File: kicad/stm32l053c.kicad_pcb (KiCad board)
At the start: 2 copper layers, 53 x 35 mm, 32 parts, among them P1 SWD, P2 PWR, Q1 Q_NMOS_GSD, SW1 SW_PUSH, SW2 SW_PUSH, SW3 SW_PUSH, U1 STM32L053C8_LQFP48, U2 TLV61225, Y1 Crystal

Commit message: Enclosure sizes
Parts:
- added REF**: MountingHole_2.2mm_M2, Mounting_Holes:MountingHole_2.2mm_M2, F.Cu at (152.0, 118.1)
- added REF**: MountingHole_2.2mm_M2, Mounting_Holes:MountingHole_2.2mm_M2, F.Cu at (131.0, 118.1)
- added REF**: MountingHole_2.2mm_M2, Mounting_Holes:MountingHole_2.2mm_M2, F.Cu at (154.0, 104.6)
- added REF**: MountingHole_2.2mm_M2, Mounting_Holes:MountingHole_2.2mm_M2, F.Cu at (132.0, 104.6)
- DS1: footprint theapi:ZEBRA-12 -> ZEBRA-12
- moved SW3 2.09 mm to (164.0, 111.6)
- moved SW1 0.78 mm to (121.5, 111.6)
- moved SW2 0.78 mm to (141.5, 111.6)

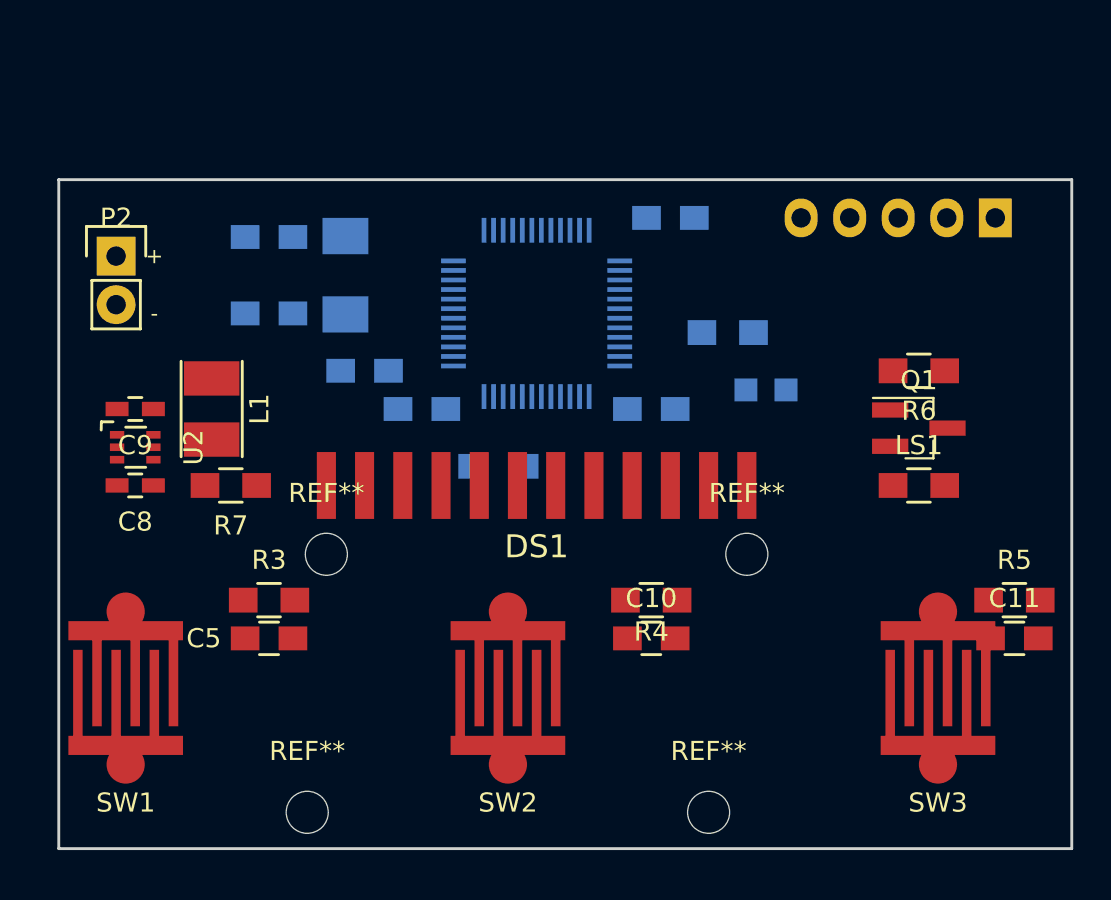
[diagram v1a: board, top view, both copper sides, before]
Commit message: Layout to fit the enclosure
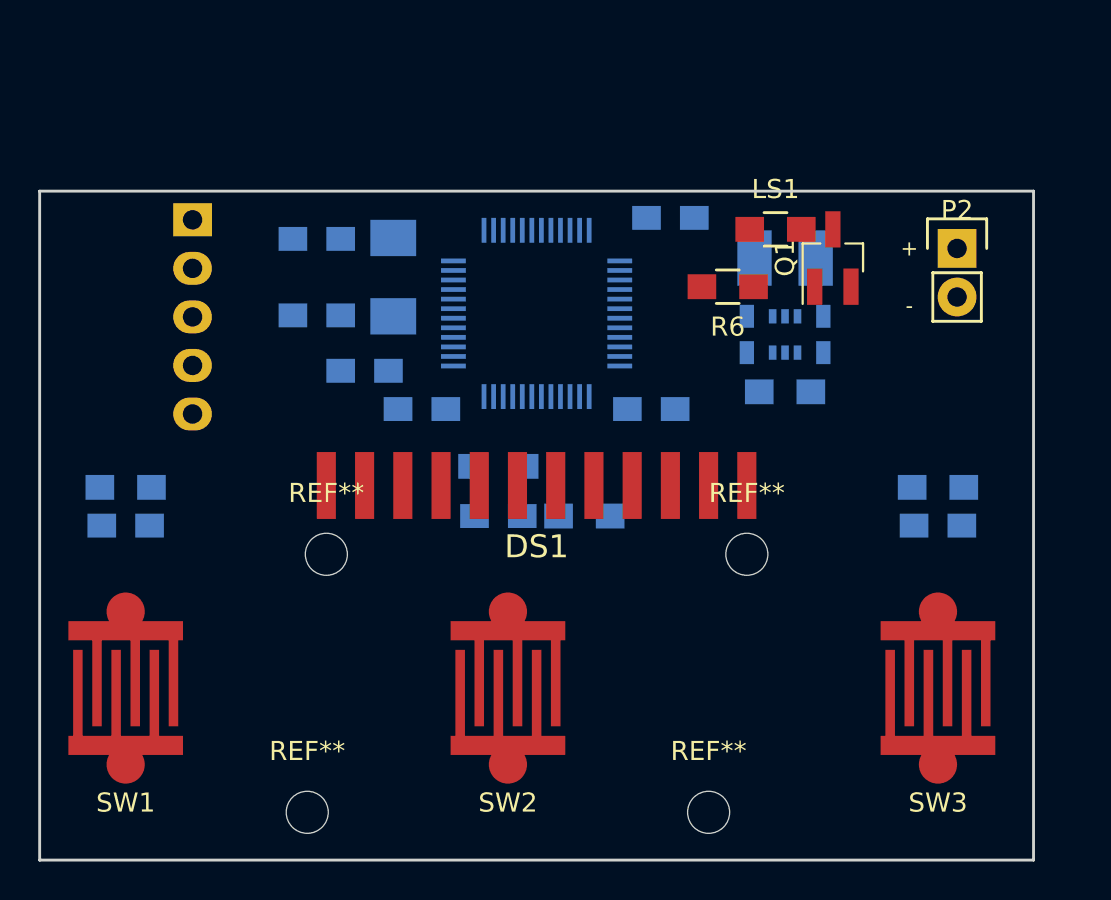
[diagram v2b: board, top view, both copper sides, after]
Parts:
- removed D1: LED, LEDs:LED_0805
- removed R1: 820, Resistors_SMD:R_0805_HandSoldering
- C10, C11, C5, C8, C9, L1, R3, R4, R5, R7, U2: moved to B.Cu
- moved P2 44.0 mm to (165.0, 88.6)
- moved P1 42.0 mm to (125.0, 87.1), turned to 180 degrees
- moved C9 36.2 mm to (158.0, 93.1), turned to 270 degrees
- moved U2 34.5 mm to (156.0, 93.1), turned to 180 degrees
- moved C8 33.0 mm to (154.0, 93.1), turned to 270 degrees
- moved L1 31.0 mm to (156.0, 89.1), turned to 180 degrees
- moved R7 29.4 mm to (156.0, 96.1)
- moved REF** 15.4 mm to (143.0, 108.6)
- moved LS1 15.4 mm to (155.5, 87.6)
- moved R6 10.9 mm to (153.0, 90.6)
- moved C10 10.2 mm to (141.0, 102.6), turned to 180 degrees
- moved Q1 9.97 mm to (158.5, 89.1), turned to 90 degrees
- moved C5 9.54 mm to (121.5, 103.1), turned to 180 degrees
- moved R3 9.54 mm to (121.5, 101.1), turned to 180 degrees
- moved C11 7.13 mm to (164.0, 103.1)
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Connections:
- U1 pad 10: (no net) -> Net-(U1-Pad10)
- U1 pad 14: (no net) -> Net-(U1-Pad14)
- U1 pad 2: (no net) -> Net-(U1-Pad2)
- U1 pad 20: (no net) -> Net-(U1-Pad20)
- U1 pad 21: (no net) -> Net-(U1-Pad21)
- U1 pad 22: (no net) -> Net-(U1-Pad22)
- U1 pad 25: (no net) -> Net-(U1-Pad25)
- U1 pad 26: (no net) -> Net-(U1-Pad26)
- U1 pad 27: (no net) -> Net-(U1-Pad27)
- U1 pad 32: (no net) -> Net-(U1-Pad32)
- U1 pad 33: (no net) -> Net-(U1-Pad33)
- U1 pad 38: (no net) -> Net-(U1-Pad38)
- U1 pad 43: (no net) -> Net-(U1-Pad43)
- U1 pad 45: (no net) -> Net-(U1-Pad45)
- U1 pad 5: (no net) -> Net-(U1-Pad5)
- U1 pad 6: (no net) -> Net-(U1-Pad6)
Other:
- board size 53 x 35 mm -> 52 x 35 mm

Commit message: Layout (WIP)
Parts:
- added D1: D_Schottky, Diodes_SMD:D_0805, B.Cu at (126.0, 100.6)
- added D2: D_Schottky, Diodes_SMD:D_0805, B.Cu at (154.0, 96.6)
- added D3: D_Schottky, Diodes_SMD:D_0805, B.Cu at (159.0, 101.6)
- added D4: D, Diodes_SMD:D_0805, F.Cu at (162.0, 89.6)
- added R1: 0, Resistors_SMD:R_0805_HandSoldering, F.Cu at (151.0, 92.6)
- added U3: um66t, TO_SOT_Packages_THT:TO-92_Inline_Narrow_Oval, F.Cu at (164.0, 96.6)
- DS1: footprint ZEBRA-12 -> theapi:ZEBRA-12
- Q1: value Q_NMOS_GSD -> Q_PNP_BEC
- R2: moved to F.Cu
- SW3: footprint SW_PCB -> theapi:SW_PCB
- moved L1 29.8 mm to (126.5, 93.1), turned to 270 degrees
- moved C9 27.6 mm to (130.5, 91.1), turned to 0 degrees
- moved U2 25.5 mm to (130.5, 93.1), turned to 270 degrees
- moved C8 23.6 mm to (130.5, 95.1), turned to 0 degrees
- moved R7 22.7 mm to (133.5, 93.1), turned to 90 degrees
- moved C10 19.3 mm to (159.2, 96.1)
- moved C4 17.2 mm to (150.0, 88.6), turned to 180 degrees
- moved R4 14.5 mm to (159.3, 98.3)
- moved R2 11.6 mm to (143.0, 88.6)
- moved Y1 9.62 mm to (137.0, 80.6)
- moved C6 9.06 mm to (132.5, 83.1)
- moved C7 9.06 mm to (132.5, 79.1)
- moved U1 0.60 mm to (143.0, 92.6), turned to 180 degrees
- moved P1 0.50 mm to (125.0, 87.6), turned to 270 degrees
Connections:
- LS1 pad 1: VDD -> +BATT
- R6 pad 2: /PB15 -> Net-(R1-Pad1)
- U1 pad 10: Net-(U1-Pad10) -> /WAKEUP_PIN1
- U1 pad 14: Net-(U1-Pad14) -> (no net)
- U1 pad 15: PA5 -> (no net)
- U1 pad 2: Net-(U1-Pad2) -> (no net)
- U1 pad 20: Net-(U1-Pad20) -> (no net)
- U1 pad 21: Net-(U1-Pad21) -> (no net)
- U1 pad 22: Net-(U1-Pad22) -> /BUZZER
- U1 pad 25: Net-(U1-Pad25) -> (no net)
- U1 pad 26: Net-(U1-Pad26) -> (no net)
- U1 pad 27: Net-(U1-Pad27) -> (no net)
- U1 pad 28: /PB15 -> /MELODY
- U1 pad 32: Net-(U1-Pad32) -> (no net)
- U1 pad 33: Net-(U1-Pad33) -> (no net)
- U1 pad 38: Net-(U1-Pad38) -> (no net)
- U1 pad 43: Net-(U1-Pad43) -> (no net)
- U1 pad 45: Net-(U1-Pad45) -> (no net)
- U1 pad 5: Net-(U1-Pad5) -> (no net)
- U1 pad 6: Net-(U1-Pad6) -> (no net)
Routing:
- net /LCD_COM2: track 0.00 -> 19.1 mm, vias 0 -> 1
- net /LCD_SEG0: track 0.00 -> 17.8 mm, vias 0 -> 1
- net /LCD_SEG6: track 0.00 -> 17.7 mm, vias 0 -> 1
- net /LCD_SEG2: track 0.00 -> 16.6 mm, vias 0 -> 1
- net /LCD_COM3: track 0.00 -> 16.6 mm, vias 0 -> 1
- net /LCD_SEG7: track 0.00 -> 16.4 mm, vias 0 -> 1
- net /LCD_SEG1: track 0.00 -> 15.6 mm, vias 0 -> 1
- net /LCD_SEG3: track 0.00 -> 11.8 mm, vias 0 -> 1
- net /LCD_SEG5: track 0.00 -> 11.8 mm, vias 0 -> 1
- net /LCD_COM0: track 0.00 -> 11.6 mm, vias 0 -> 1
- net /LCD_COM1: track 0.00 -> 11.2 mm, vias 0 -> 1
- net /LCD_SEG4: track 0.00 -> 8.05 mm, vias 0 -> 1

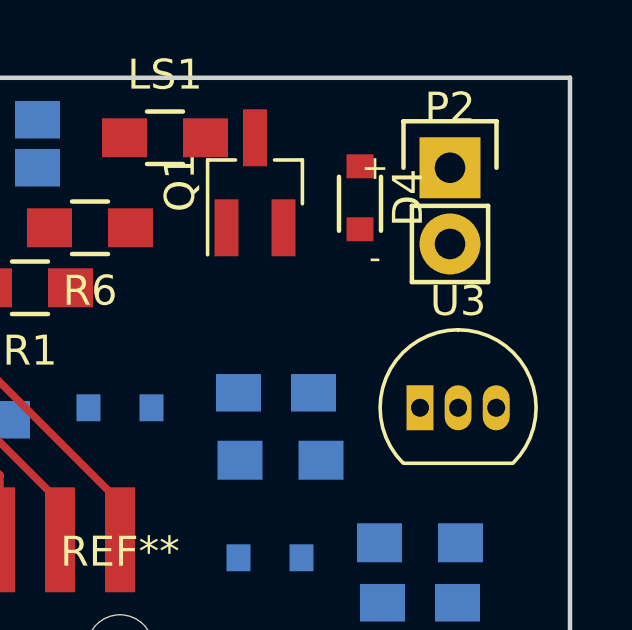
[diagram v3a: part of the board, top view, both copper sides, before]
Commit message: Fixed the melody output
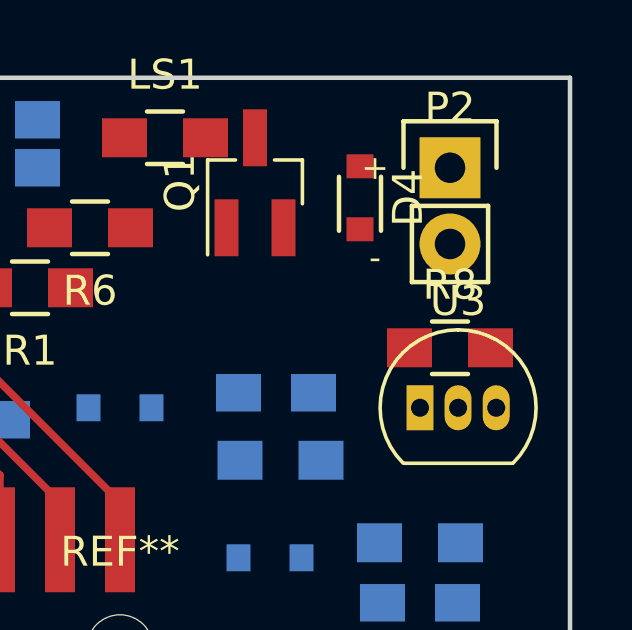
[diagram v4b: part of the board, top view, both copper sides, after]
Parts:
- added R8: 1K, Resistors_SMD:R_0805_HandSoldering, F.Cu at (165.0, 94.6)
- R6: value 1K -> 220
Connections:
- U1 pad 14: (no net) -> Net-(U1-Pad14)
- U1 pad 15: (no net) -> PA5
- U1 pad 2: (no net) -> Net-(U1-Pad2)
- U1 pad 20: (no net) -> Net-(U1-Pad20)
- U1 pad 21: (no net) -> Net-(U1-Pad21)
- U1 pad 25: (no net) -> /MELODY
- U1 pad 26: (no net) -> Net-(U1-Pad26)
- U1 pad 27: (no net) -> Net-(U1-Pad27)
- U1 pad 28: /MELODY -> Net-(U1-Pad28)
- U1 pad 32: (no net) -> Net-(U1-Pad32)
- U1 pad 33: (no net) -> Net-(U1-Pad33)
- U1 pad 38: (no net) -> Net-(U1-Pad38)
- U1 pad 43: (no net) -> Net-(U1-Pad43)
- U1 pad 45: (no net) -> Net-(U1-Pad45)
- U1 pad 5: (no net) -> Net-(U1-Pad5)
- U1 pad 6: (no net) -> Net-(U1-Pad6)
- U3 pad 2: /MELODY -> Net-(R8-Pad1)
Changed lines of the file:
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@@
 (kicad_pcb (version 4) (host pcbnew 4.0.5-e0-6337~49~ubuntu16.04.1)
   (general
-    (links 108)
-    (no_connects 102)
+    (links 109)
+    (no_connects 91)
     (area 116.924999 85.524999 169.075001 120.675001)
     (thickness 1.6)
@@
     (tracks 73)
     (zones 0)
-    (modules 40)
-    (nets 37)
+    (modules 41)
+    (nets 53)
   )
   (page A4)
@@
   (net 35 /BUZZER)
   (net 36 /MELODY)
+  (net 37 "Net-(R8-Pad1)")
+  (net 38 "Net-(U1-Pad2)")
+  (net 39 "Net-(U1-Pad5)")
+  (net 40 "Net-(U1-Pad6)")
+  (net 41 "Net-(U1-Pad14)")
+  (net 42 PA5)
+  (net 43 "Net-(U1-Pad20)")
+  (net 44 "Net-(U1-Pad21)")
+  (net 45 "Net-(U1-Pad26)")
+  (net 46 "Net-(U1-Pad27)")
+  (net 47 "Net-(U1-Pad28)")
+  (net 48 "Net-(U1-Pad32)")
+  (net 49 "Net-(U1-Pad33)")
+  (net 50 "Net-(U1-Pad38)")
+  (net 51 "Net-(U1-Pad43)")
+  (net 52 "Net-(U1-Pad45)")
   (net_class Default "This is the default net class."
     (clearance 0.2032)
@@
     (add_net "Net-(R4-Pad2)")
     (add_net "Net-(R5-Pad2)")
+    (add_net "Net-(R8-Pad1)")
+    (add_net "Net-(U1-Pad14)")
+    (add_net "Net-(U1-Pad2)")
+    (add_net "Net-(U1-Pad20)")
+    (add_net "Net-(U1-Pad21)")
+    (add_net "Net-(U1-Pad26)")
+    (add_net "Net-(U1-Pad27)")
+    (add_net "Net-(U1-Pad28)")
+    (add_net "Net-(U1-Pad32)")
+    (add_net "Net-(U1-Pad33)")
+    (add_net "Net-(U1-Pad38)")
+    (add_net "Net-(U1-Pad43)")
+    (add_net "Net-(U1-Pad45)")
+    (add_net "Net-(U1-Pad5)")
+    (add_net "Net-(U1-Pad6)")
+    (add_net PA5)
     (add_net SWCLK)
     (add_net SWDIO)
@@
     (pad 1 smd rect (at -4.35 2.75 180) (size 1.3 0.25) (layers B.Cu B.Paste B.Mask)
       (net 6 /VLCD))
-    (pad 2 smd rect (at -4.35 2.25 180) (size 1.3 0.25) (layers B.Cu B.Paste B.Mask))
+    (pad 2 smd rect (at -4.35 2.25 180) (size 1.3 0.25) (layers B.Cu B.Paste B.Mask)
+      (net 38 "Net-(U1-Pad2)"))
     (pad 3 smd rect (at -4.35 1.75 180) (size 1.3 0.25) (layers B.Cu B.Paste B.Mask)
       (net 8 /OSC32_IN))
     (pad 4 smd rect (at -4.35 1.25 180) (size 1.3 0.25) (layers B.Cu B.Paste B.Mask)
       (net 9 /OSC32_OUT))
-    (pad 5 smd rect (at -4.35 0.75 180) (size 1.3 0.25) (layers B.Cu B.Paste B.Mask))
-    (pad 6 smd rect (at -4.35 0.25 180) (size 1.3 0.25) (layers B.Cu B.Paste B.Mask))
+    (pad 5 smd rect (at -4.35 0.75 180) (size 1.3 0.25) (layers B.Cu B.Paste B.Mask)
+      (net 39 "Net-(U1-Pad5)"))
+    (pad 6 smd rect (at -4.35 0.25 180) (size 1.3 0.25) (layers B.Cu B.Paste B.Mask)
+      (net 40 "Net-(U1-Pad6)"))
     (pad 7 smd rect (at -4.35 -0.25 180) (size 1.3 0.25) (layers B.Cu B.Paste B.Mask)
       (net 5 NRST))
@@
     (pad 13 smd rect (at -2.75 -4.35 90) (size 1.3 0.25) (layers B.Cu B.Paste B.Mask)
       (net 18 /LCD_SEG2))
-    (pad 14 smd rect (at -2.25 -4.35 90) (size 1.3 0.25) (layers B.Cu B.Paste B.Mask))
-    (pad 15 smd rect (at -1.75 -4.35 90) (size 1.3 0.25) (layers B.Cu B.Paste B.Mask))
+    (pad 14 smd rect (at -2.25 -4.35 90) (size 1.3 0.25) (layers B.Cu B.Paste B.Mask)
+      (net 41 "Net-(U1-Pad14)"))
+    (pad 15 smd rect (at -1.75 -4.35 90) (size 1.3 0.25) (layers B.Cu B.Paste B.Mask)
+      (net 42 PA5))
     (pad 16 smd rect (at -1.25 -4.35 90) (size 1.3 0.25) (layers B.Cu B.Paste B.Mask)
       (net 19 /LCD_SEG3))
@@
     (pad 19 smd rect (at 0.25 -4.35 90) (size 1.3 0.25) (layers B.Cu B.Paste B.Mask)
       (net 22 /LCD_SEG6))
-    (pad 20 smd rect (at 0.75 -4.35 90) (size 1.3 0.25) (layers B.Cu B.Paste B.Mask))
-    (pad 21 smd rect (at 1.25 -4.35 90) (size 1.3 0.25) (layers B.Cu B.Paste B.Mask))
+    (pad 20 smd rect (at 0.75 -4.35 90) (size 1.3 0.25) (layers B.Cu B.Paste B.Mask)
+      (net 43 "Net-(U1-Pad20)"))
+    (pad 21 smd rect (at 1.25 -4.35 90) (size 1.3 0.25) (layers B.Cu B.Paste B.Mask)
+      (net 44 "Net-(U1-Pad21)"))
     (pad 22 smd rect (at 1.75 -4.35 90) (size 1.3 0.25) (layers B.Cu B.Paste B.Mask)
       (net 35 /BUZZER))
@@
     (pad 24 smd rect (at 2.75 -4.35 90) (size 1.3 0.25) (layers B.Cu B.Paste B.Mask)
       (net 1 VDD))
-    (pad 25 smd rect (at 4.35 -2.75 180) (size 1.3 0.25) (layers B.Cu B.Paste B.Mask))
-    (pad 26 smd rect (at 4.35 -2.25 180) (size 1.3 0.25) (layers B.Cu B.Paste B.Mask))
-    (pad 27 smd rect (at 4.35 -1.75 180) (size 1.3 0.25) (layers B.Cu B.Paste B.Mask))
+    (pad 25 smd rect (at 4.35 -2.75 180) (size 1.3 0.25) (layers B.Cu B.Paste B.Mask)
+      (net 36 /MELODY))
+    (pad 26 smd rect (at 4.35 -2.25 180) (size 1.3 0.25) (layers B.Cu B.Paste B.Mask)
+      (net 45 "Net-(U1-Pad26)"))
+    (pad 27 smd rect (at 4.35 -1.75 180) (size 1.3 0.25) (layers B.Cu B.Paste B.Mask)
+      (net 46 "Net-(U1-Pad27)"))
     (pad 28 smd rect (at 4.35 -1.25 180) (size 1.3 0.25) (layers B.Cu B.Paste B.Mask)
-      (net 36 /MELODY))
+      (net 47 "Net-(U1-Pad28)"))
     (pad 29 smd rect (at 4.35 -0.75 180) (size 1.3 0.25) (layers B.Cu B.Paste B.Mask)
       (net 14 /LCD_COM0))
@@
     (pad 31 smd rect (at 4.35 0.25 180) (size 1.3 0.25) (layers B.Cu B.Paste B.Mask)
       (net 24 /LCD_COM2))
-    (pad 32 smd rect (at 4.35 0.75 180) (size 1.3 0.25) (layers B.Cu B.Paste B.Mask))
-    (pad 33 smd rect (at 4.35 1.25 180) (size 1.3 0.25) (layers B.Cu B.Paste B.Mask))
+    (pad 32 smd rect (at 4.35 0.75 180) (size 1.3 0.25) (layers B.Cu B.Paste B.Mask)
+      (net 48 "Net-(U1-Pad32)"))
+    (pad 33 smd rect (at 4.35 1.25 180) (size 1.3 0.25) (layers B.Cu B.Paste B.Mask)
+      (net 49 "Net-(U1-Pad33)"))
     (pad 34 smd rect (at 4.35 1.75 180) (size 1.3 0.25) (layers B.Cu B.Paste B.Mask)
       (net 4 SWDIO))
@@
     (pad 37 smd rect (at 2.75 4.35 90) (size 1.3 0.25) (layers B.Cu B.Paste B.Mask)
       (net 3 SWCLK))
-    (pad 38 smd rect (at 2.25 4.35 90) (size 1.3 0.25) (layers B.Cu B.Paste B.Mask))
+    (pad 38 smd rect (at 2.25 4.35 90) (size 1.3 0.25) (layers B.Cu B.Paste B.Mask)
+      (net 50 "Net-(U1-Pad38)"))
     (pad 39 smd rect (at 1.75 4.35 90) (size 1.3 0.25) (layers B.Cu B.Paste B.Mask)
       (net 23 /LCD_SEG7))
@@
     (pad 42 smd rect (at 0.25 4.35 90) (size 1.3 0.25) (layers B.Cu B.Paste B.Mask)
       (net 13 /BUTTON2))
-    (pad 43 smd rect (at -0.25 4.35 90) (size 1.3 0.25) (layers B.Cu B.Paste B.Mask))
+    (pad 43 smd rect (at -0.25 4.35 90) (size 1.3 0.25) (layers B.Cu B.Paste B.Mask)
+      (net 51 "Net-(U1-Pad43)"))
     (pad 44 smd rect (at -0.75 4.35 90) (size 1.3 0.25) (layers B.Cu B.Paste B.Mask)
       (net 28 "Net-(R2-Pad1)"))
-    (pad 45 smd rect (at -1.25 4.35 90) (size 1.3 0.25) (layers B.Cu B.Paste B.Mask))
+    (pad 45 smd rect (at -1.25 4.35 90) (size 1.3 0.25) (layers B.Cu B.Paste B.Mask)
+      (net 52 "Net-(U1-Pad45)"))
     (pad 46 smd rect (at -1.75 4.35 90) (size 1.3 0.25) (layers B.Cu B.Paste B.Mask)
       (net 25 /LCD_COM3))
@@
       (effects (font (size 1 1) (thickness 0.15)))
     )
-    (fp_text value 1K (at 0 2.1 180) (layer F.Fab)
+    (fp_text value 220 (at 0 2.1 180) (layer F.Fab)
       (effects (font (size 1 1) (thickness 0.15)))
     )
@@
     (fp_arc (start 1.27 0) (end 1.27 -2.6) (angle 135) (layer F.SilkS) (width 0.12))
     (pad 2 thru_hole oval (at 1.27 0 180) (size 0.89916 1.50114) (drill 0.6) (layers *.Cu *.Mask)
-      (net 36 /MELODY))
+      (net 37 "Net-(R8-Pad1)"))
     (pad 3 thru_hole oval (at 2.54 0 180) (size 0.89916 1.50114) (drill 0.6) (layers *.Cu *.Mask)
       (net 2 Earth))
@@
     )
   )
+  (module Resistors_SMD:R_0805_HandSoldering (layer F.Cu)
+    (at 165 94.6)
+    (descr "Resistor SMD 0805, hand soldering")
+    (tags "resistor 0805")
+    (attr smd)
+    (fp_text reference R8 (at 0 -2.1) (layer F.SilkS)
+      (effects (font (size 1 1) (thickness 0.15)))
+    )
+    (fp_text value 1K (at 0 2.1) (layer F.Fab)
+      (effects (font (size 1 1) (thickness 0.15)))
+    )
+    (fp_line (start -1 0.625) (end -1 -0.625) (layer F.Fab) (width 0.1))
+    (fp_line (start 1 0.625) (end -1 0.625) (layer F.Fab) (width 0.1))
+    (fp_line (start 1 -0.625) (end 1 0.625) (layer F.Fab) (width 0.1))
+    (fp_line (start -1 -0.625) (end 1 -0.625) (layer F.Fab) (width 0.1))
+    (fp_line (start -2.4 -1) (end 2.4 -1) (layer F.CrtYd) (width 0.05))
+    (fp_line (start -2.4 1) (end 2.4 1) (layer F.CrtYd) (width 0.05))
+    (fp_line (start -2.4 -1) (end -2.4 1) (layer F.CrtYd) (width 0.05))
+    (fp_line (start 2.4 -1) (end 2.4 1) (layer F.CrtYd) (width 0.05))
+    (fp_line (start 0.6 0.875) (end -0.6 0.875) (layer F.SilkS) (width 0.15))
+    (fp_line (start -0.6 -0.875) (end 0.6 -0.875) (layer F.SilkS) (width 0.15))
+    (pad 1 smd rect (at -1.35 0) (size 1.5 1.3) (layers F.Cu F.Paste F.Mask)
+      (net 37 "Net-(R8-Pad1)"))
+    (pad 2 smd rect (at 1.35 0) (size 1.5 1.3) (layers F.Cu F.Paste F.Mask)
+      (net 36 /MELODY))
+    (model Resistors_SMD.3dshapes/R_0805_HandSoldering.wrl
+      (at (xyz 0 0 0))
+      (scale (xyz 1 1 1))
+      (rotate (xyz 0 0 0))
+    )
+  )

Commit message: PNP & more layout
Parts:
- removed D4: D, Diodes_SMD:D_0805
- D1, D2, D3: footprint Diodes_SMD:D_0805 -> Diodes_SMD:SOD-523
- Q1: value Q_PNP_BEC -> BC807
- R8: value 1K -> 0
- U2: footprint TO_SOT_Packages_SMD:SC-70-6 -> theapi:SC-70-6
- moved P2 46.2 mm to (119.0, 92.6)
- moved U3 41.1 mm to (124.0, 87.1)
- moved LS1 35.2 mm to (120.3, 87.1)
- moved Q1 31.1 mm to (127.5, 92.1), turned to 180 degrees
- moved P1 29.9 mm to (154.9, 87.1)
- moved C7 29.9 mm to (159.0, 92.8), turned to 270 degrees
- moved R6 25.3 mm to (128.0, 94.6)
- moved C6 23.5 mm to (154.0, 92.6), turned to 90 degrees
- moved R1 23.3 mm to (128.0, 96.6), turned to 0 degrees
- moved Y1 22.9 mm to (156.5, 92.6)
- moved D2 2.66 mm to (155.5, 98.8), turned to 270 degrees
- moved D1 1.80 mm to (125.0, 102.1), turned to 270 degrees
- moved D3 1.58 mm to (160.5, 102.1), turned to 270 degrees
- moved C10 1.57 mm to (158.8, 97.6), turned to 0 degrees
- moved R4 1.43 mm to (158.7, 99.6)
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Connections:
- C3 pad 1: VDD -> /VDDA
- LS1 pad 1: +BATT -> Net-(LS1-Pad1)
- LS1 pad 2: Net-(D4-Pad2) -> Earth
- Q1 pad 2: Earth -> +BATT
- Q1 pad 3: Net-(D4-Pad2) -> Net-(LS1-Pad1)
- R8 pad 1: Net-(R8-Pad1) -> /VDDA
- R8 pad 2: /MELODY -> VDD
- U1 pad 9: VDD -> /VDDA
- U3 pad 2: Net-(R8-Pad1) -> /MELODY
